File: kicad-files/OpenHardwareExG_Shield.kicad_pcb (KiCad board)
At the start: 4 copper layers, 190 parts, among them P1 CONN_1, P10 CONN_18, P11 CONN_1, P12 CONN_1, P13 CONN_1, P14 CONN_1, P15 CONN_1, P16 CONN_1, P17 CONN_1, P18 CONN_1, P19 ARDUINO_SHIELD, P2 CONN_1, P20 CONN_3X2, P21 CONN_3X2, P22 CONN_7, P23 CONN_1, P24 CONN_1, P25 CONN_1, P26 CONN_1, P27 CONN_1, P28 CONN_1, P29 CONN_1, P3 CONN_1, P30 CONN_1, P31 CONN_1, P32 CONN_1, P33 CONN_1, P34 CONN_1, P35 CONN_1, P36 CONN_1, P37 CONN_1, P38 CONN_1, P39 CONN_1, P4 CONN_1, P40 CONN_1, P41 CONN_1, P42 CONN_1, P43 CONN_1, P44 CONN_1, P45 CONN_1, P46 CONN_1, P47 CONN_1, P48 CONN_1, P49 CONN_1, P5 CONN_1, P50 CONN_1, P51 CONN_1, P52 CONN_1, P53 CONN_1, P54 CONN_1, P55 CONN_1, P6 CONN_1, P7 CONN_1, P8 CONN_1, P9 CONN_1, U1 ADS1299, U2 BT1308W-600D, U3 TL431BIDBZR, U4 873-AAT3220IGY-33T1, U5 ADUM6000, U6 SI8663, U7 74LS02, U8 74LS00, U9 74LS125

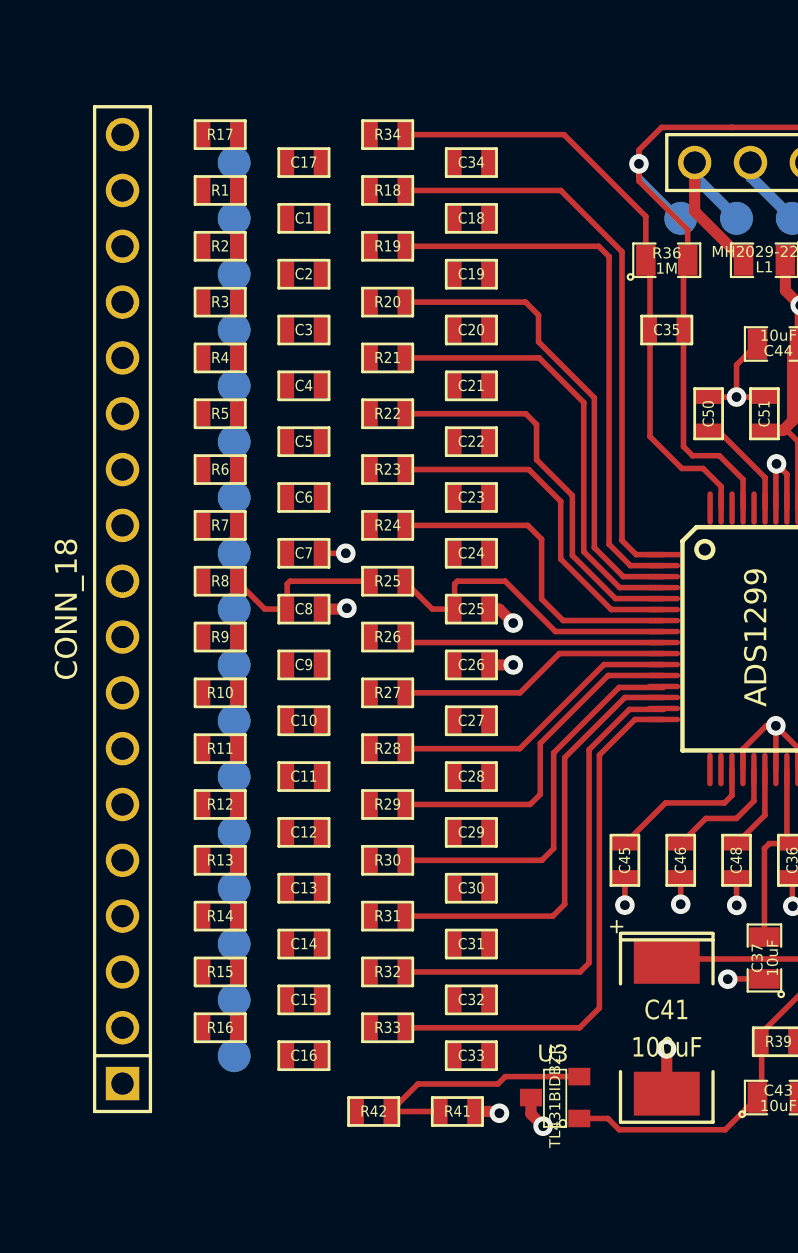
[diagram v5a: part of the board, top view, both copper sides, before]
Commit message: connect the EEG inputs to the chip, via the filter
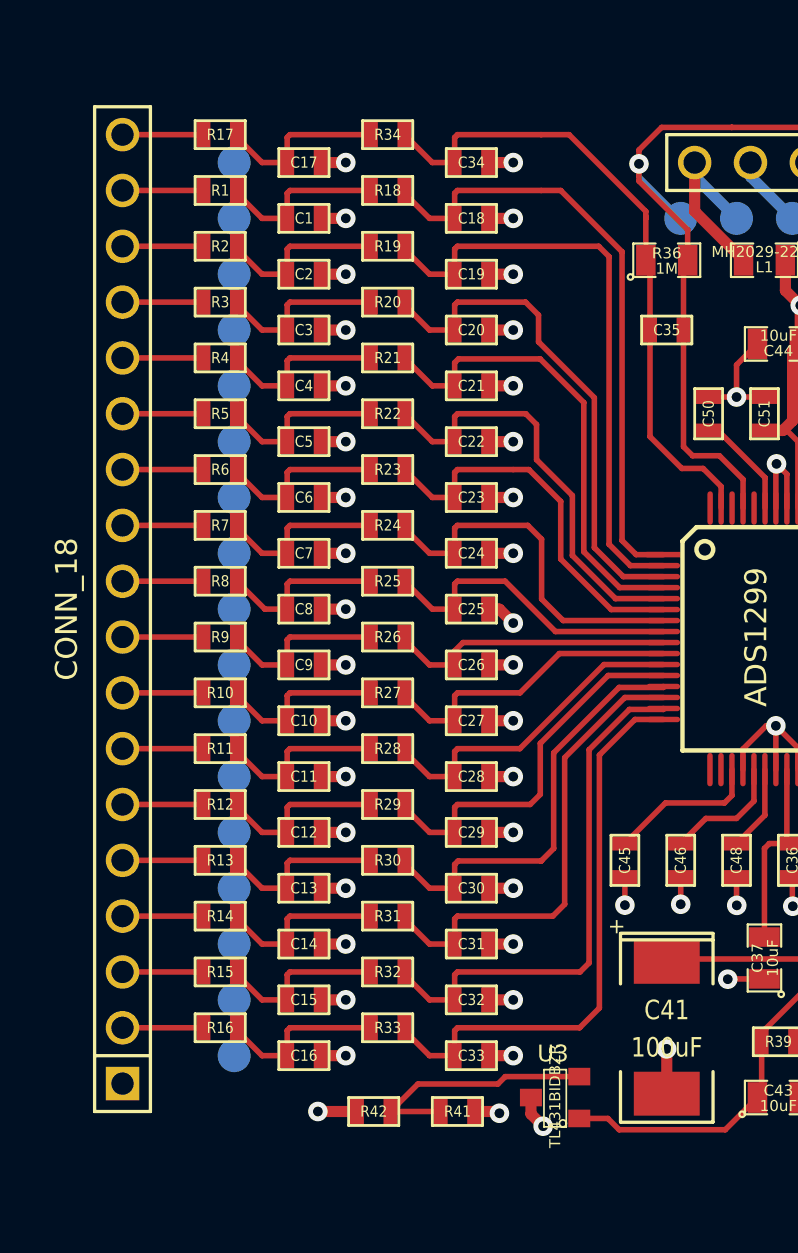
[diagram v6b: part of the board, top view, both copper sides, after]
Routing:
- net AGND: track 55.4 -> 91.4 mm, vias 21 -> 52
- net N-0000030: track 0.00 -> 7.89 mm
- net N-0000010: track 0.00 -> 7.89 mm
- net N-000006: track 0.00 -> 7.89 mm
- net N-0000056: track 0.00 -> 7.89 mm
- net N-0000031: track 0.00 -> 7.89 mm
- net N-0000018: track 0.00 -> 7.89 mm
- net N-0000016: track 0.00 -> 7.89 mm
- net N-0000013: track 0.00 -> 7.89 mm
- net N-0000012: track 0.00 -> 7.89 mm
- net N-000009: track 0.00 -> 7.89 mm
- net N-0000063: track 0.00 -> 7.89 mm
- net N-0000033: track 0.00 -> 7.89 mm
- net N-000003: track 0.00 -> 7.89 mm
- net N-000002: track 0.00 -> 7.89 mm
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
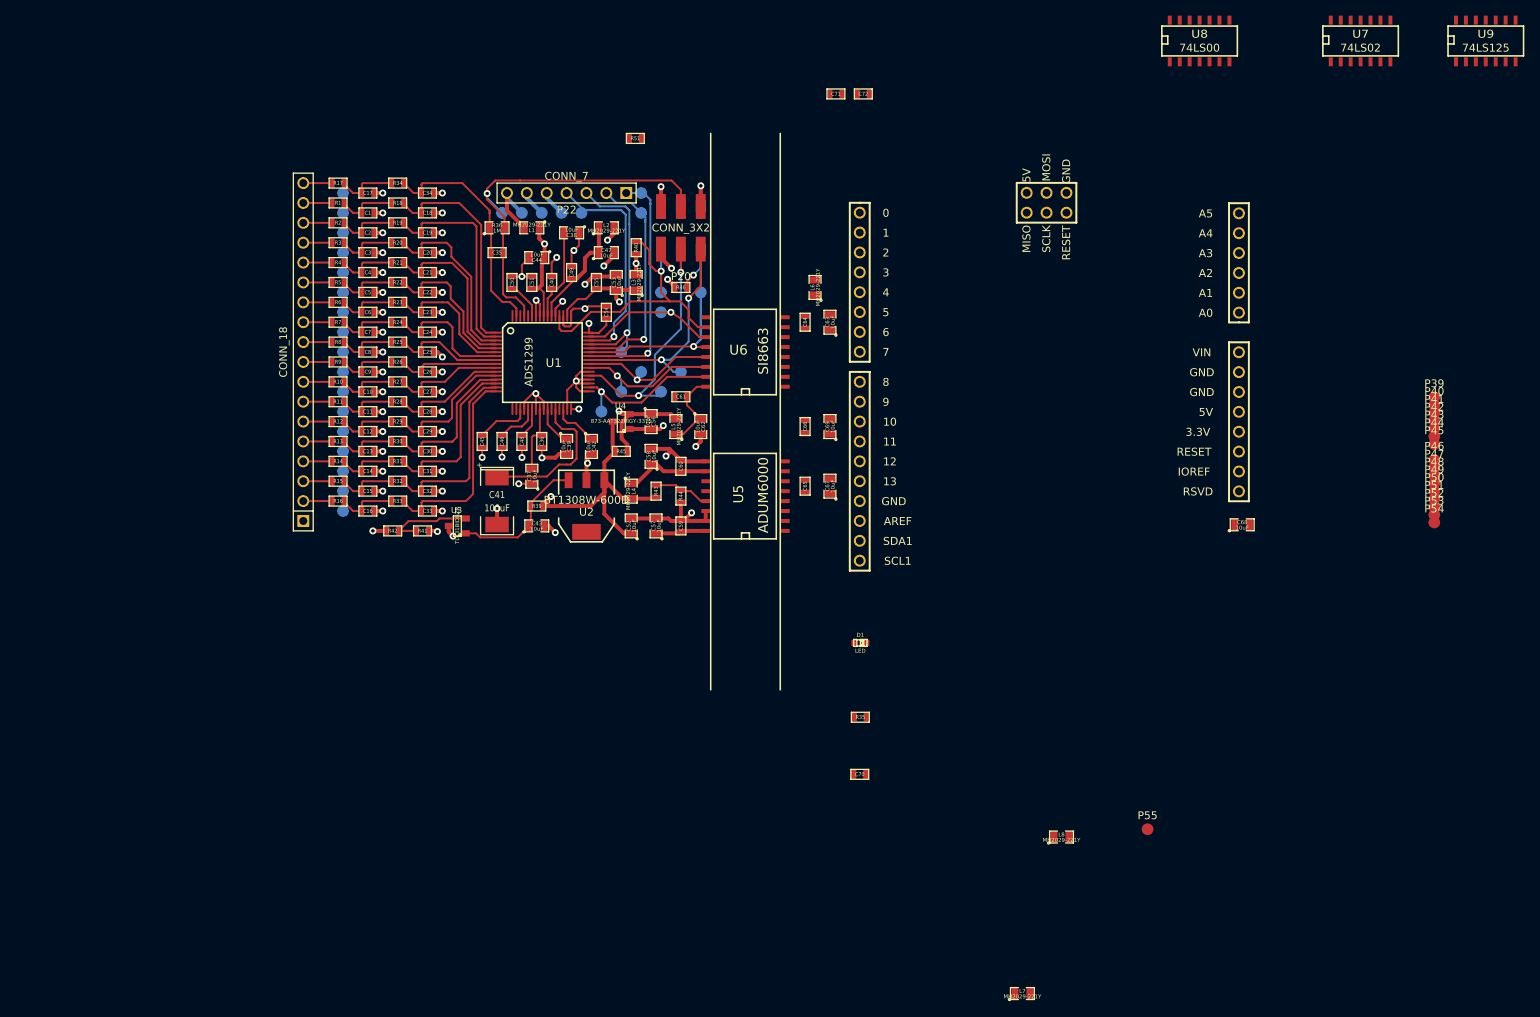
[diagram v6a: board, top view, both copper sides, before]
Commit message: sketch placement of pre-isolated logic
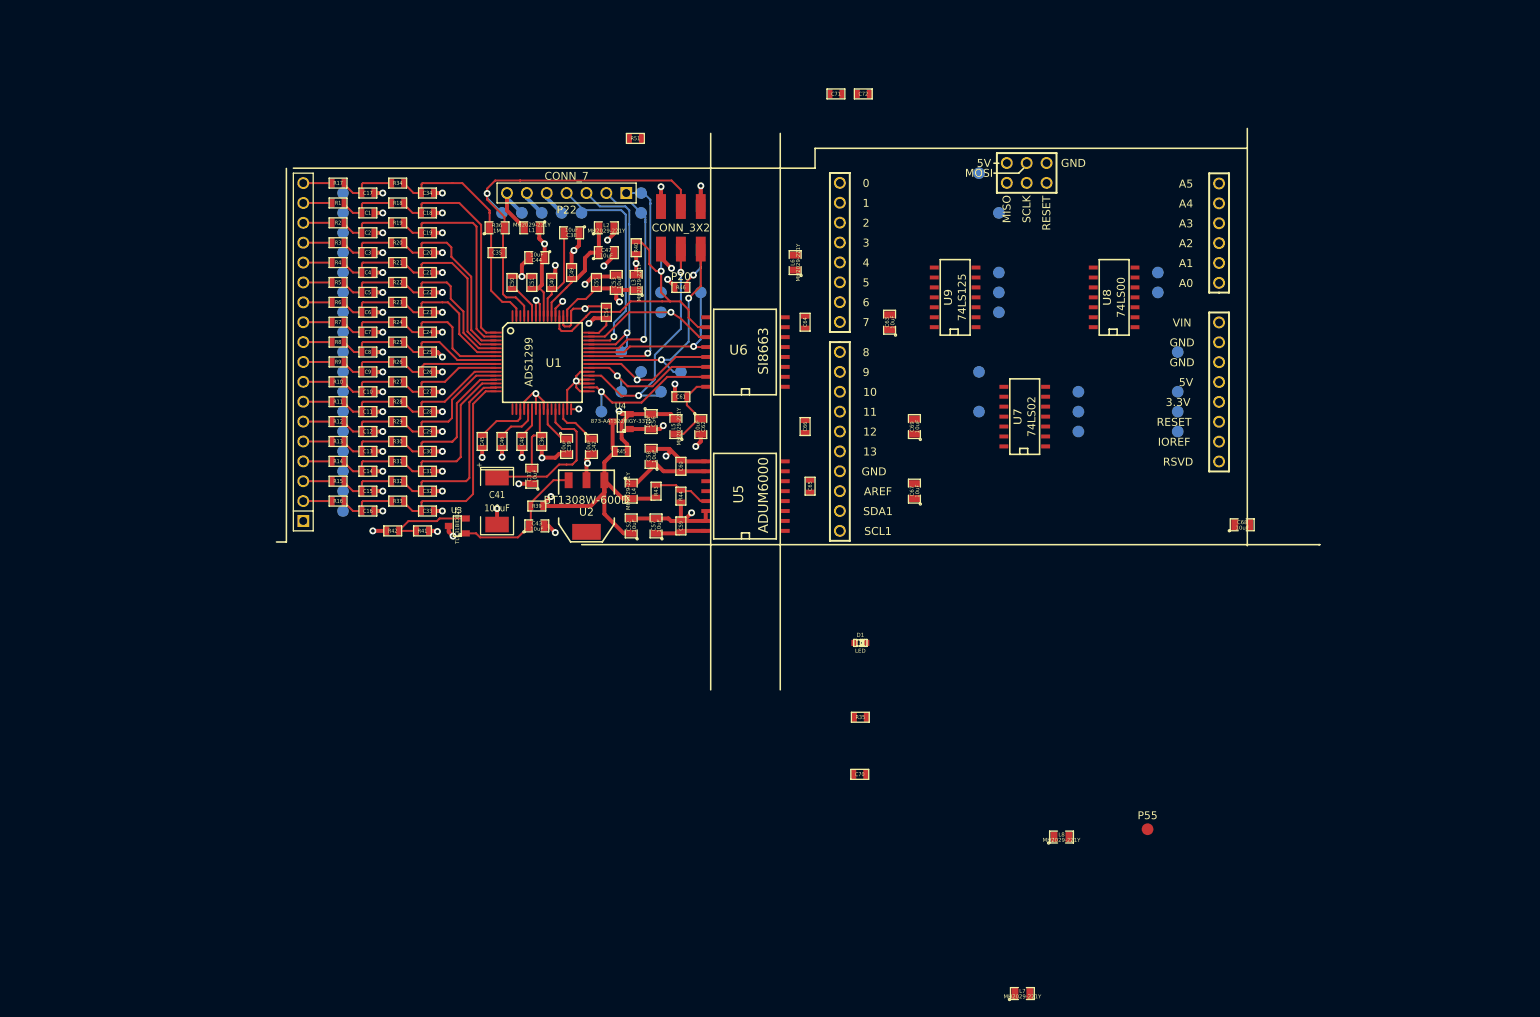
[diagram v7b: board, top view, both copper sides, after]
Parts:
- P39, P40, P41, P42, P43, P44, P45, P46, P47, P48, P49, P50, P51, P52, P53, P54: moved to B.Cu
- moved U9 75.5 mm to (146.7, 51.4), turned to 90 degrees
- moved P54 73.3 mm to (149.9, 35.6)
- moved P53 67.7 mm to (152.4, 40.6)
- moved U7 64.6 mm to (155.6, 66.7), turned to 90 degrees
- moved P52 63.2 mm to (152.4, 48.3)
- moved P45 58.9 mm to (152.4, 50.8)
- moved P40 58.3 mm to (149.9, 61.0)
- moved P42 58.2 mm to (149.9, 66.0)
- moved P44 57.9 mm to (152.4, 53.3)
- moved P51 47.5 mm to (162.6, 63.5)
- moved P50 46.1 mm to (162.6, 68.6)
- moved P39 45.5 mm to (162.6, 66.0)
- moved P41 39.6 mm to (172.7, 48.3)
- moved P43 39.4 mm to (172.7, 50.8)
- moved P49 36.8 mm to (175.3, 58.4)
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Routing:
- net DGND: track 69.2 -> 70.8 mm, vias 10 -> 11
- net +3.3VADC: track 18.7 -> 20.0 mm
- net AGND: track 91.4 -> 90.1 mm

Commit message: ground planes on isolated side of board
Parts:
- removed R51: R, SM0603
- P55: moved to B.Cu
- moved P55 80.5 mm to (154.9, 40.6)
- moved L7 67.2 mm to (175.3, 76.2)
- moved D1 49.6 mm to (180.3, 76.2)
- moved C70 41.5 mm to (154.9, 76.2)
- moved L8 41.3 mm to (147.3, 81.3)
- moved R35 31.5 mm to (147.3, 76.2)
- moved C71 15.9 mm to (127.0, 40.6)
- moved C72 15.0 mm to (127.0, 38.1)
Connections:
- C52 pad 2: DGND -> AGND
- C53 pad 2: DGND -> AGND
- C54 pad 2: DGND -> AGND
- C55 pad 2: DGND -> AGND
- C56 pad 2: DGND -> AGND
- C57 pad 2: DGND -> AGND
- C58 pad 2: DGND -> AGND
- C59 pad 2: DGND -> AGND
- C60 pad 2: DGND -> AGND
- C61 pad 2: DGND -> AGND
- C62 pad 2: DGND -> AGND
- P20 pad 1: DGND -> AGND
- P20 pad 5: DGND -> AGND
- P20 pad 6: DGND -> AGND
- P21 pad 1: DGND -> AGND
- P21 pad 5: DGND -> AGND
- R44 pad 1: DGND -> AGND
- U1 pad 31: DGND -> AGND
- U1 pad 33: DGND -> AGND
- U1 pad 35: DGND -> AGND
- U1 pad 36: DGND -> AGND
- U1 pad 38: DGND -> AGND
- U1 pad 49: DGND -> AGND
- U1 pad 51: DGND -> AGND
- U4 pad 1: DGND -> AGND
- U5 pad 14: DGND -> AGND
- U5 pad 15: DGND -> AGND
- U5 pad 9: DGND -> AGND
- U6 pad 9: DGND -> AGND
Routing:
- net AGND: track 90.1 -> 162.6 mm, vias 52 -> 64
- net DGND: track 70.8 -> 0.00 mm, vias 11 -> 0
- net /BIASINV: track 50.2 -> 54.4 mm, vias 1 -> 2
- added copper zone on Inner1.Cu, net AGND
- removed copper zone on Inner2.Cu, net +3.3VADC
- removed copper zone on Inner1.Cu, net DGND
